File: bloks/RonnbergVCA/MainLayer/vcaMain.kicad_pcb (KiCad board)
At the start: 2 copper layers, 91.4 x 45.7 mm, 38 parts, among them J1 Conn_02x03_Odd_Even, J10 Conn_02x03_Odd_Even, J11 Conn_02x03_Odd_Even, J12 Conn_02x03_Odd_Even, J1M1 Conn_01x01, J2 Conn_02x03_Odd_Even, J2M1 Conn_01x01, J3 Conn_02x03_Odd_Even, J3M1 Conn_01x01, J4 Conn_02x03_Odd_Even, J4M1 Conn_01x01, J5 Conn_02x03_Odd_Even, J5M1 Conn_01x01, J6 Conn_02x03_Odd_Even, J6M1 Conn_01x01, J7 Conn_02x03_Odd_Even, J7M1 Conn_01x01, J8 Conn_02x03_Odd_Even, J9 Conn_02x03_Odd_Even, U1 TL072, U2 CA3080

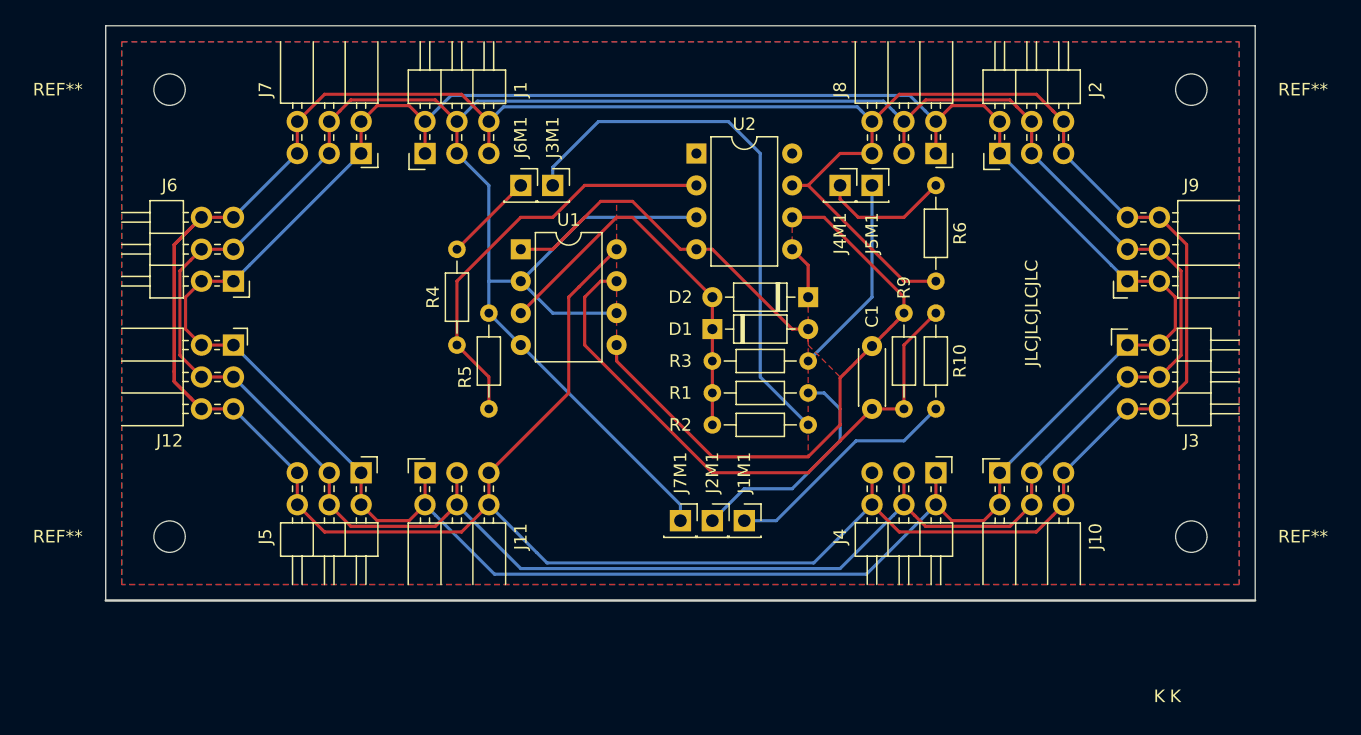
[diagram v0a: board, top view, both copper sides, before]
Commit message: Added -12v rail to power headers
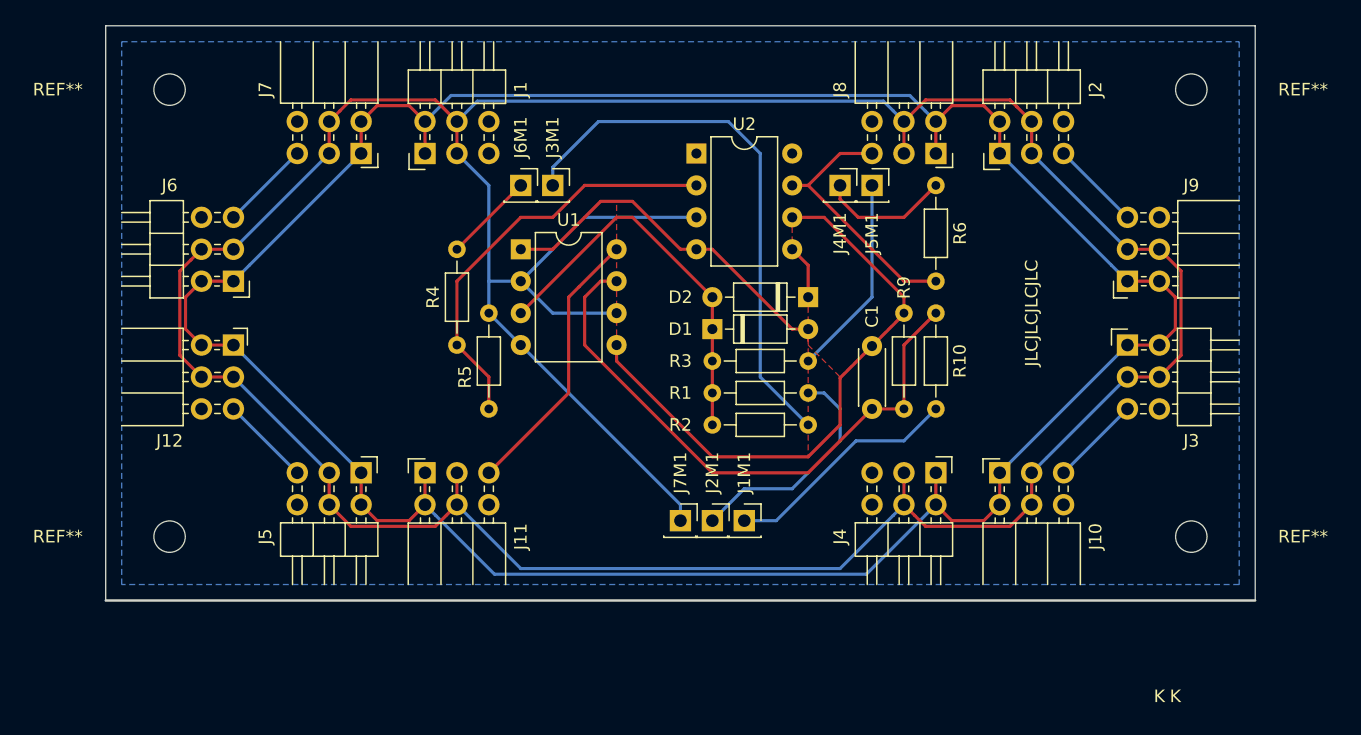
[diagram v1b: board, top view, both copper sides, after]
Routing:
- net +12V: track 287.0 -> 71.4 mm
- removed copper zone on F.Cu, net GND
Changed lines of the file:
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@@
     (thickness 1.6)
     (drawings 7)
-    (tracks 231)
+    (tracks 185)
     (zones 0)
     (modules 38)
@@
   (segment (start 156.21 86.36) (end 163.83 93.98) (width 0.25) (layer F.Cu) (net 14))
   (segment (start 156.21 86.36) (end 154.94 86.36) (width 0.25) (layer F.Cu) (net 14))
-  (segment (start 160.440001 80.430001) (end 161.29 81.28) (width 0.25) (layer B.Cu) (net 14))
-  (segment (start 160.114999 80.104999) (end 160.440001 80.430001) (width 0.25) (layer B.Cu) (net 14))
-  (segment (start 131.985001 80.104999) (end 160.114999 80.104999) (width 0.25) (layer B.Cu) (net 14))
-  (segment (start 130.81 81.28) (end 131.985001 80.104999) (width 0.25) (layer B.Cu) (net 14))
   (segment (start 110.49 104.14) (end 115.57 109.22) (width 0.25) (layer B.Cu) (net 14))
   (segment (start 110.49 88.9) (end 115.57 83.82) (width 0.25) (layer B.Cu) (net 14))
-  (segment (start 134.62 115.57) (end 130.81 111.76) (width 0.25) (layer B.Cu) (net 14))
-  (segment (start 135.43999 116.38999) (end 134.62 115.57) (width 0.25) (layer B.Cu) (net 14))
-  (segment (start 161.29 111.76) (end 156.66001 116.38999) (width 0.25) (layer B.Cu) (net 14))
-  (segment (start 156.66001 116.38999) (end 135.43999 116.38999) (width 0.25) (layer B.Cu) (net 14))
   (segment (start 176.53 109.22) (end 181.61 104.14) (width 0.25) (layer B.Cu) (net 14))
   (segment (start 181.61 88.9) (end 176.53 83.82) (width 0.25) (layer B.Cu) (net 14))
-  (segment (start 175.680001 80.430001) (end 176.53 81.28) (width 0.25) (layer F.Cu) (net 14))
-  (segment (start 174.359981 79.109981) (end 175.680001 80.430001) (width 0.25) (layer F.Cu) (net 14))
-  (segment (start 163.460019 79.109981) (end 174.359981 79.109981) (width 0.25) (layer F.Cu) (net 14))
-  (segment (start 161.29 81.28) (end 163.460019 79.109981) (width 0.25) (layer F.Cu) (net 14))
-  (segment (start 184.999999 103.290001) (end 184.15 104.14) (width 0.25) (layer F.Cu) (net 14))
-  (segment (start 186.320019 101.969981) (end 184.999999 103.290001) (width 0.25) (layer F.Cu) (net 14))
-  (segment (start 186.320019 91.070019) (end 186.320019 101.969981) (width 0.25) (layer F.Cu) (net 14))
-  (segment (start 184.15 88.9) (end 186.320019 91.070019) (width 0.25) (layer F.Cu) (net 14))
-  (segment (start 175.680001 112.609999) (end 176.53 111.76) (width 0.25) (layer F.Cu) (net 14))
-  (segment (start 174.359982 113.930018) (end 175.680001 112.609999) (width 0.25) (layer F.Cu) (net 14))
-  (segment (start 163.460018 113.930018) (end 174.359982 113.930018) (width 0.25) (layer F.Cu) (net 14))
-  (segment (start 161.29 111.76) (end 163.460018 113.930018) (width 0.25) (layer F.Cu) (net 14))
-  (segment (start 117.74002 113.93002) (end 115.57 111.76) (width 0.25) (layer F.Cu) (net 14))
-  (segment (start 130.81 111.76) (end 128.63998 113.93002) (width 0.25) (layer F.Cu) (net 14))
-  (segment (start 128.63998 113.93002) (end 117.74002 113.93002) (width 0.25) (layer F.Cu) (net 14))
-  (segment (start 105.77998 91.07002) (end 105.77998 101.168982) (width 0.25) (layer F.Cu) (net 14))
-  (segment (start 107.95 88.9) (end 105.77998 91.07002) (width 0.25) (layer F.Cu) (net 14))
-  (segment (start 105.77998 101.96998) (end 105.77998 101.168982) (width 0.25) (layer F.Cu) (net 14))
-  (segment (start 107.95 104.14) (end 105.77998 101.96998) (width 0.25) (layer F.Cu) (net 14))
-  (segment (start 107.100001 103.290001) (end 107.95 104.14) (width 0.25) (layer F.Cu) (net 14))
-  (segment (start 105.779981 101.969981) (end 107.100001 103.290001) (width 0.25) (layer F.Cu) (net 14))
-  (segment (start 105.779981 91.070019) (end 105.779981 101.969981) (width 0.25) (layer F.Cu) (net 14))
-  (segment (start 107.95 88.9) (end 105.779981 91.070019) (width 0.25) (layer F.Cu) (net 14))
-  (segment (start 117.74002 79.10998) (end 115.57 81.28) (width 0.25) (layer F.Cu) (net 14))
-  (segment (start 130.81 81.28) (end 128.63998 79.10998) (width 0.25) (layer F.Cu) (net 14))
-  (segment (start 128.63998 79.10998) (end 117.74002 79.10998) (width 0.25) (layer F.Cu) (net 14))
-  (segment (start 110.49 88.9) (end 107.95 88.9) (width 0.25) (layer F.Cu) (net 14))
-  (segment (start 110.49 104.14) (end 107.95 104.14) (width 0.25) (layer F.Cu) (net 14))
-  (segment (start 115.57 109.22) (end 115.57 111.76) (width 0.25) (layer F.Cu) (net 14))
-  (segment (start 130.81 111.76) (end 130.81 109.22) (width 0.25) (layer F.Cu) (net 14))
-  (segment (start 161.29 111.76) (end 161.29 109.22) (width 0.25) (layer F.Cu) (net 14))
-  (segment (start 176.53 111.76) (end 176.53 109.22) (width 0.25) (layer F.Cu) (net 14))
-  (segment (start 181.61 104.14) (end 184.15 104.14) (width 0.25) (layer F.Cu) (net 14))
-  (segment (start 184.15 88.9) (end 181.61 88.9) (width 0.25) (layer F.Cu) (net 14))
-  (segment (start 176.53 83.82) (end 176.53 81.28) (width 0.25) (layer F.Cu) (net 14))
-  (segment (start 161.29 83.82) (end 161.29 81.28) (width 0.25) (layer F.Cu) (net 14))
-  (segment (start 130.81 81.28) (end 130.81 83.82) (width 0.25) (layer F.Cu) (net 14))
-  (segment (start 115.57 83.82) (end 115.57 81.28) (width 0.25) (layer F.Cu) (net 14))
   (segment (start 156.21 86.36) (end 158.75 83.82) (width 0.25) (layer F.Cu) (net 14))
   (segment (start 158.75 83.82) (end 161.29 83.82) (width 0.25) (layer F.Cu) (net 14))
@@
     (connect_pads (clearance 0.508))
     (min_thickness 0.254)
-    (fill yes (arc_segments 16) (thermal_gap 0.508) (thermal_bridge_width 0.508))
-    (polygon
-      (pts
-        (xy 190.5 74.93) (xy 190.5 118.11) (xy 101.6 118.11) (xy 101.6 74.93)
-      )
-    )
-  )
-  (zone (net 17) (net_name GND) (layer F.Cu) (hatch edge 0.508)
-    (connect_pads (clearance 0.508))
-    (min_thickness 0.254)
